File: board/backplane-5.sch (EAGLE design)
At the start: 146 parts, among them CN1 RJ45JACK90, CN2 4PINCONNFEMALE-1.6, CN3 4PINCONNFEMALE-1.6, CN4 4PINCONNFEMALE-1.6, CN5 4PINCONNFEMALE-1.6, CN6 4PINCONNFEMALE-1.6, U1 AMS1117-5.0, U10 RT9193, U11 KSZ9897, U12 KSZ8081MLX, U13 STM32F217-100, U2 AMS1117-5.0, U3 AMS1117-5.0, U4 AMS1117-5.0, U5 AMS1117-5.0, U6 AMS1117-2.5, U7 AMS1117-1.2, U8 RT9193, U9 AMS1117-5.0, Y1 25MHz, Y2 25MHz, Y3 25MHz

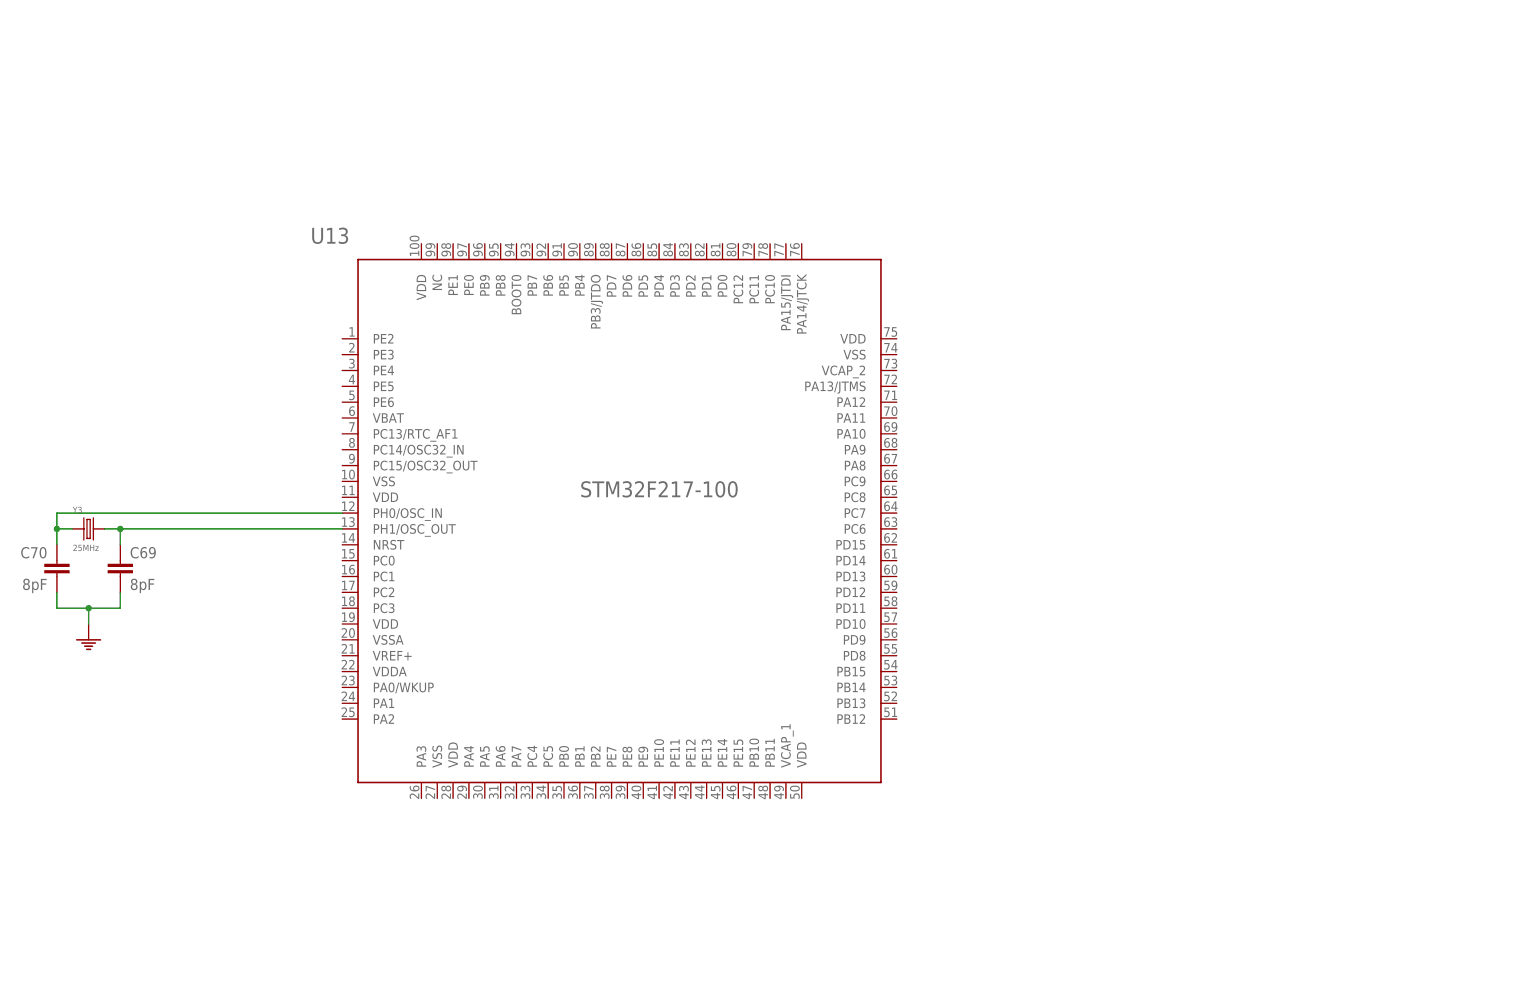
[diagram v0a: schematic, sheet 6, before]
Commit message: Added power to the STM32 and its decoupling caps
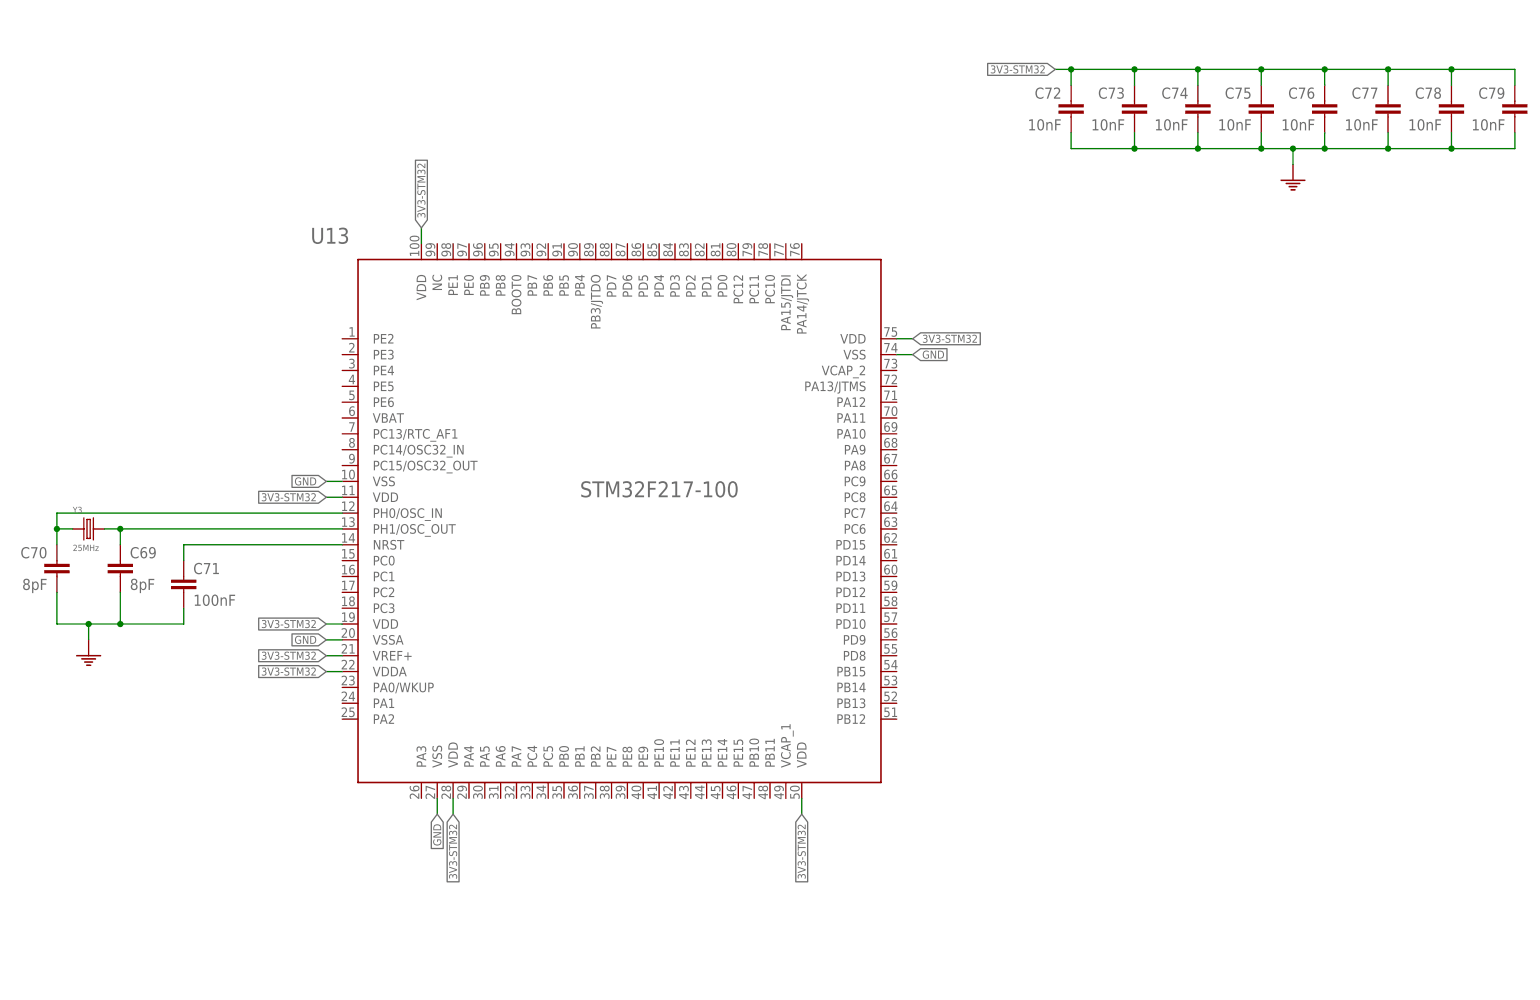
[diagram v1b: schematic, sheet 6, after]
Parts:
- added C71: 100nF, tuetuopay:C0603
- added C72, C73, C74, C75, C76, C77, C78, C79: 10nF, tuetuopay:C0603
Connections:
- new net N$23: C71.1, U13.NRST
- net 3V3-STM32: now also C72.1, C73.1, C74.1, C75.1, C76.1, C77.1, C78.1, C79.1, U13.VDD@1, U13.VDD@2, U13.VDD@3, U13.VDD@4, U13.VDD@5, U13.VDD@6, U13.VDDA@1, U13.VREF+
- net GND: now also C71.2, C72.2, C73.2, C74.2, C75.2, C76.2, C77.2, C78.2, C79.2, U13.VSS@1, U13.VSS@2, U13.VSS@3, U13.VSSA@1

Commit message: Added VCAP capacitors
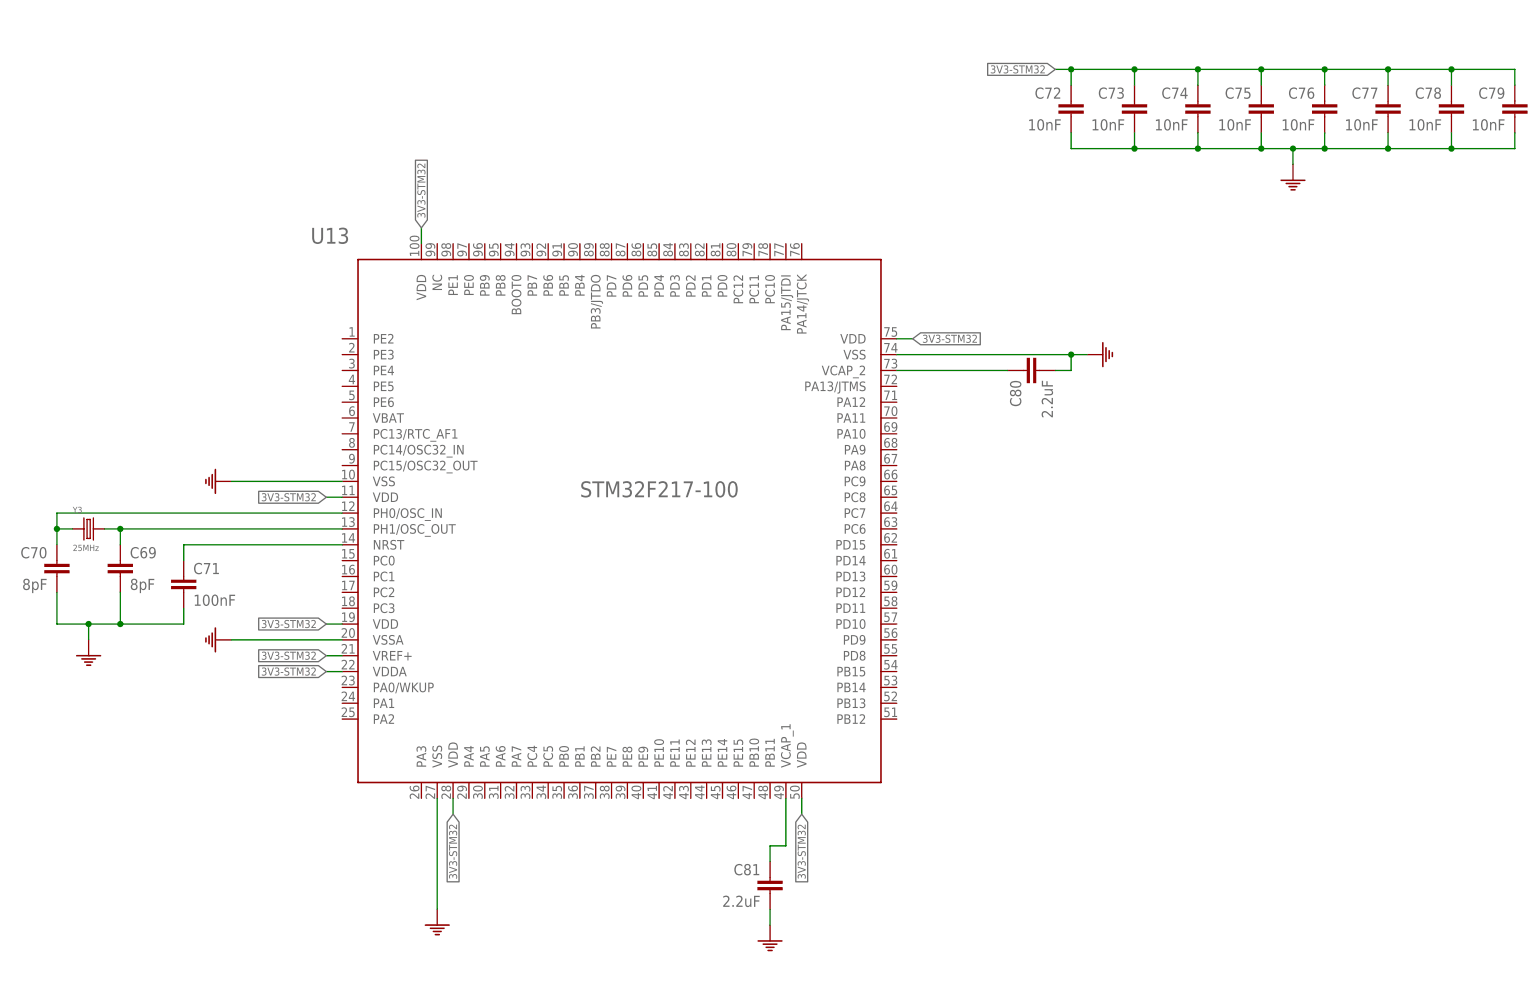
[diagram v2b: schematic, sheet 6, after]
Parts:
- added C80, C81: 2.2uF, tuetuopay:C0805
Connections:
- new net N$34: C80.1, U13.VCAP_2
- new net N$35: C81.1, U13.VCAP_1
- net GND: now also C80.2, C81.2

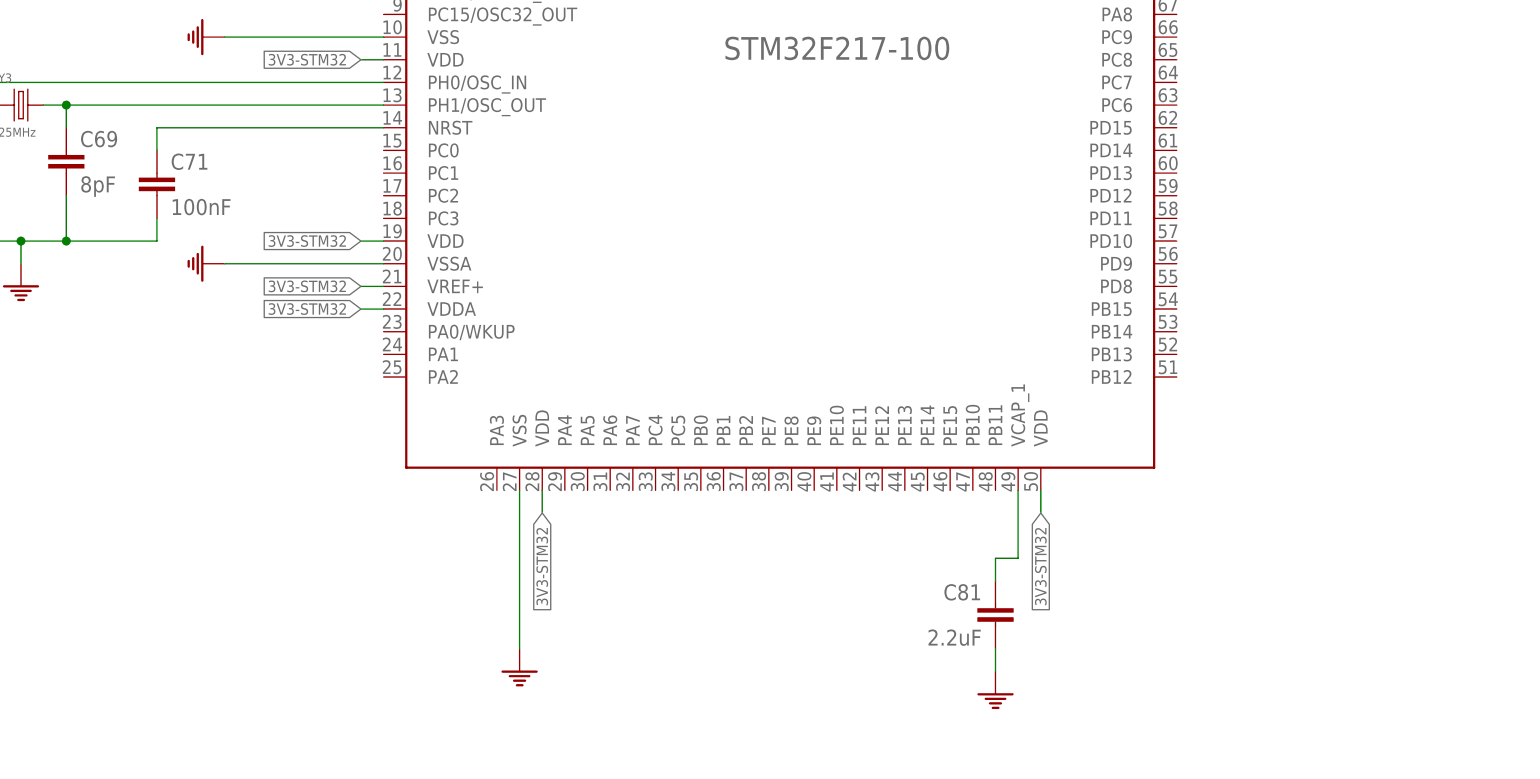
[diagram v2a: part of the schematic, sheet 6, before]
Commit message: Added switch <-> stm32 rmii in schematic
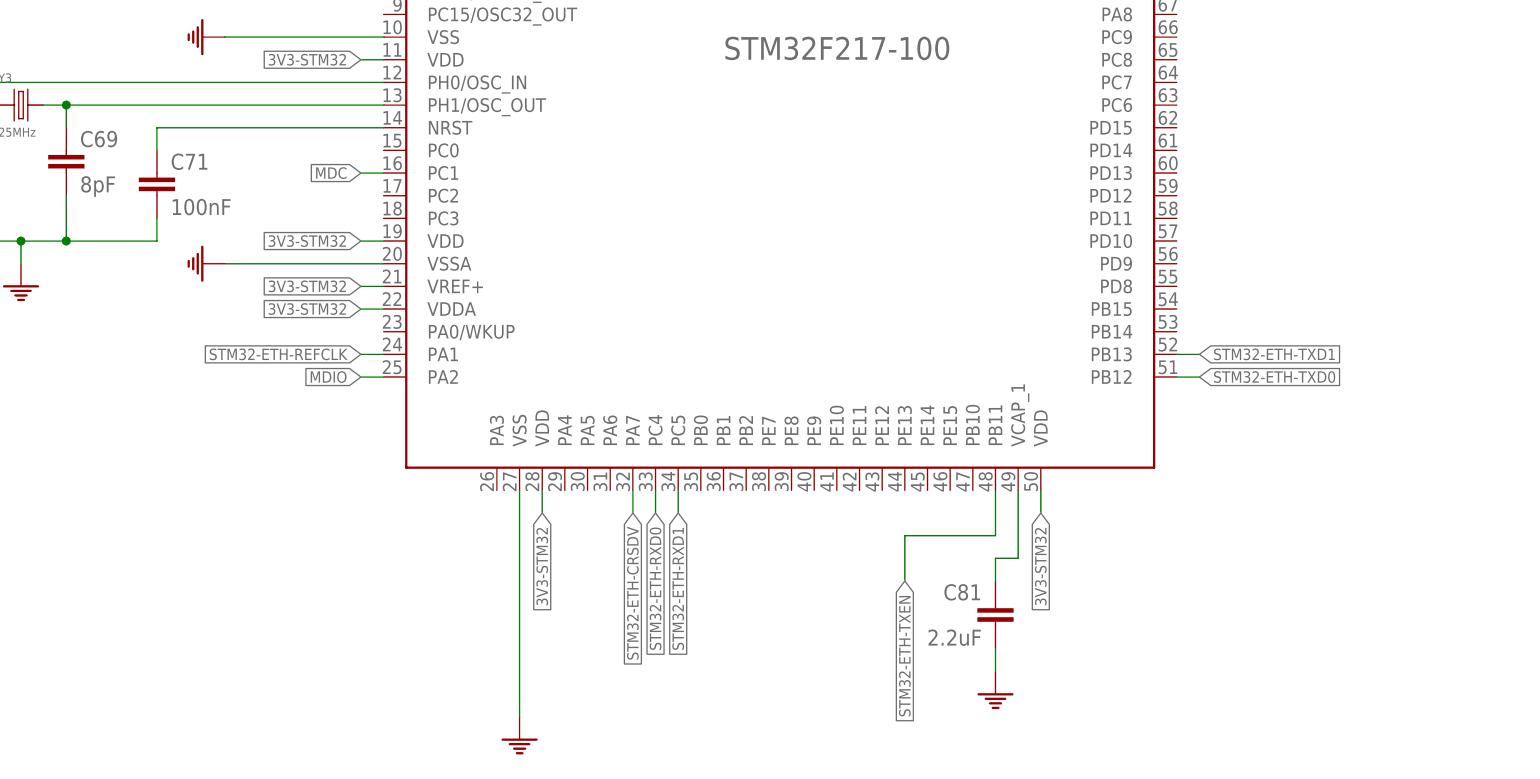
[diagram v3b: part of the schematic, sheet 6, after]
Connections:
- new net STM32-ETH-CRSDV: U11.RX_DV7/CRS_DV7/RX_CTL7, U13.PA7
- new net STM32-ETH-REFCLK: U11.TX_CLK7/REFCLKI7, U13.PA1
- new net STM32-ETH-RXD0: U11.RXD7_0, U13.PC4
- new net STM32-ETH-RXD1: U11.RXD7_1, U13.PC5
- new net STM32-ETH-TXD0: U11.TXD7_0, U13.PB12
- new net STM32-ETH-TXD1: U11.TXD7_1, U13.PB13
- new net STM32-ETH-TXEN: U11.TX_EN7/TX_CTL7, U13.PB11
- net MDC: now also U13.PC1
- net MDIO: now also U13.PA2

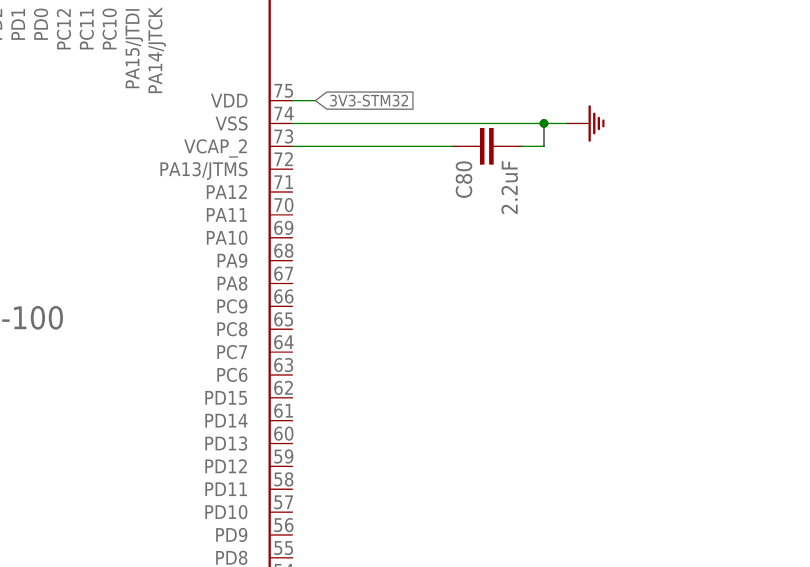
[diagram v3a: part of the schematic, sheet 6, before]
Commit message: Added the REFCLK source for switch <-> stm
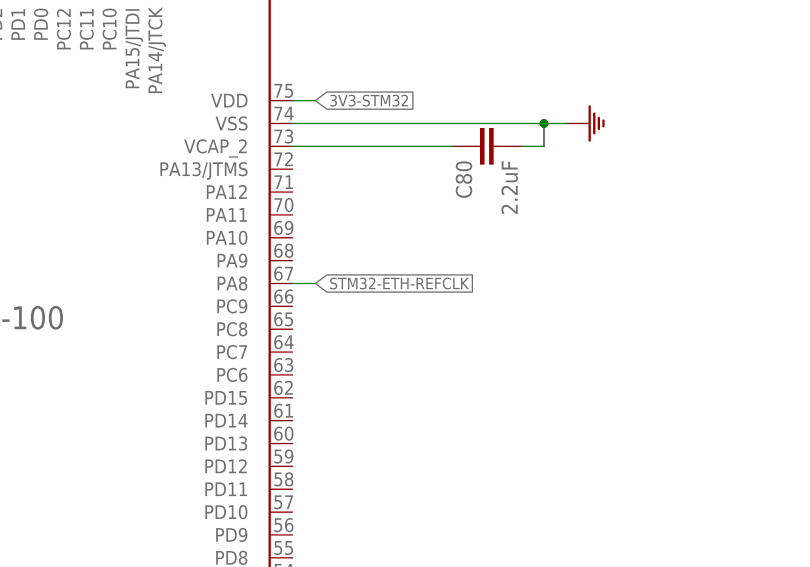
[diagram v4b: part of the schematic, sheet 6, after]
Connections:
- net STM32-ETH-REFCLK: now also U13.PA8
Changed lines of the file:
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@@
 <label x="60.96" y="66.04" size="1.27" layer="95" rot="R180" xref="yes"/>
+</segment>
+<segment>
+<pinref part="U13" gate="G$1" pin="PA8"/>
+<wire x1="152.4" y1="104.14" x2="154.94" y2="104.14" width="0.1524" layer="91"/>
+<label x="154.94" y="104.14" size="1.27" layer="95" xref="yes"/>
 </segment>
 </net>

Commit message: Proper supply symbols for some supply rails
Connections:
- net 12V renamed +12V
- net 5V renamed +5V
- removed net 2V5: C11.POS, C54.1, C55.1, C56.1, C57.1, C61.1, C62.1, L2.2, LED1.A, LED10.A, LED2.A, LED3.A, LED4.A, LED5.A, LED6.A, LED7.A, LED8.A, LED9.A, R16.2, R29.1, R30.1, R31.1, R32.2, R4.2, R7.2, R8.2, U11.VDDIO, U12.VDDIO, U6.VOUT
- new net VCCIO: C11.POS, C54.1, C55.1, C56.1, C57.1, C61.1, C62.1, C72.1, C73.1, C74.1, C75.1, C76.1, C77.1, C78.1, C79.1, L2.2, LED1.A, LED10.A, LED2.A, LED3.A, LED4.A, LED5.A, LED6.A, LED7.A, LED8.A, LED9.A, R16.2, R29.1, R30.1, R31.1, R32.2, R4.2, R6.2, R7.2, R8.2, U11.VDDIO, U12.VDDIO, U13.VDD@1, U13.VDD@2, U13.VDD@3, U13.VDD@4, U13.VDD@5, U13.VDD@6, U13.VDDA@1, U13.VREF+, U6.VOUT
- net 3V3-PHY: no longer R6.2
- net 3V3-STM32: no longer C72.1, C73.1, C74.1, C75.1, C76.1, C77.1, C78.1, C79.1, U13.VDD@1, U13.VDD@2, U13.VDD@3, U13.VDD@4, U13.VDD@5, U13.VDD@6, U13.VDDA@1, U13.VREF+
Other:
- moved on the sheet: C72, C73, C74, C75, C76, C77, C78, C79, C80, C81

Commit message: Wired Pis in Gbps and used PHY for ext jack
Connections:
- removed net PHY1->PI1_N: RJ1.3, U11.TXRX1M_B
- removed net PHY1->PI1_P: RJ1.6, U11.TXRX1P_B
- removed net PHY2->PI2_N: RJ2.3, U11.TXRX2M_B
- removed net PHY2->PI2_P: RJ2.6, U11.TXRX2P_B
- removed net PHY3->PI3_N: RJ3.3, U11.TXRX3M_B
- removed net PHY3->PI3_P: RJ3.6, U11.TXRX3P_B
- removed net PHY4->PI4_N: RJ4.3, U11.TXRX4M_B
- removed net PHY4->PI4_P: RJ4.6, U11.TXRX4P_B
- removed net PHY6->PI5_N: RJ5.3, U12.RXM
- removed net PHY6->PI5_P: RJ5.6, U12.RXP
- removed net PI1->PHY1_N: RJ1.7, U11.TXRX1M_A
- removed net PI1->PHY1_P: RJ1.8, U11.TXRX1P_A
- removed net PI2->PHY2_N: RJ2.7, U11.TXRX2M_A
- removed net PI2->PHY2_P: RJ2.8, U11.TXRX2P_A
- removed net PI3->PHY3_N: RJ3.7, U11.TXRX3M_A
- removed net PI3->PHY3_P: RJ3.8, U11.TXRX3P_A
- removed net PI4->PHY4_N: RJ4.7, U11.TXRX4M_A
- removed net PI4->PHY4_P: RJ4.8, U11.TXRX4P_A
- removed net PI5->PHY6_N: RJ5.7, U12.TXM
- removed net PI5->PHY6_P: RJ5.8, U12.TXP
- new net PHY1A_N: RJ1.2, U11.TXRX1M_A
- new net PHY1A_P: RJ1.1, U11.TXRX1P_A
- new net PHY1B_N: RJ1.6, U11.TXRX1M_B
- new net PHY1B_P: RJ1.3, U11.TXRX1P_B
- new net PHY1C_N: RJ1.5, U11.TXRX1M_C
- new net PHY1C_P: RJ1.4, U11.TXRX1P_C
- new net PHY1D_N: RJ1.8, U11.TXRX1M_D
- new net PHY1D_P: RJ1.7, U11.TXRX1P_D
- new net PHY2A_N: RJ2.2, U11.TXRX2M_A
- new net PHY2A_P: RJ2.1, U11.TXRX2P_A
- new net PHY2B_N: RJ2.6, U11.TXRX2M_B
- new net PHY2B_P: RJ2.3, U11.TXRX2P_B
- new net PHY2C_N: RJ2.5, U11.TXRX2M_C
- new net PHY2C_P: RJ2.4, U11.TXRX2P_C
- new net PHY2D_N: RJ2.8, U11.TXRX2M_D
- new net PHY2D_P: RJ2.7, U11.TXRX2P_D
- new net PHY3A_N: RJ3.2, U11.TXRX3M_A
- new net PHY3A_P: RJ3.1, U11.TXRX3P_A
- new net PHY3B_N: RJ3.6, U11.TXRX3M_B
- new net PHY3B_P: RJ3.3, U11.TXRX3P_B
- new net PHY3C_N: RJ3.5, U11.TXRX3M_C
- new net PHY3C_P: RJ3.4, U11.TXRX3P_C
- new net PHY3D_N: RJ3.8, U11.TXRX3M_D
- new net PHY3D_P: RJ3.7, U11.TXRX3P_D
- new net PHY4A_N: RJ4.2, U11.TXRX4M_A
- new net PHY4A_P: RJ4.1, U11.TXRX4P_A
- new net PHY4B_N: RJ4.6, U11.TXRX4M_B
- new net PHY4B_P: RJ4.3, U11.TXRX4P_B
- new net PHY4C_N: RJ4.5, U11.TXRX4M_C
- new net PHY4C_P: RJ4.4, U11.TXRX4P_C
- new net PHY4D_N: RJ4.8, U11.TXRX4M_D
- new net PHY4D_P: RJ4.7, U11.TXRX4P_D
- new net PHY6A_N: CN1.2, U12.RXM
- new net PHY6A_P: CN1.1, U12.RXP
- new net PHY6B_N: CN1.6, U12.TXM
- new net PHY6B_P: CN1.3, U12.TXP
- new net PHY6C_N: CN1.5
- new net PHY6C_P: CN1.4
- new net PHY6D_N: CN1.8
- new net PHY6D_P: CN1.7
- net PHY5A_N: now also RJ5.2; no longer CN1.2
- net PHY5A_P: now also RJ5.1; no longer CN1.1
- net PHY5B_N: now also RJ5.6; no longer CN1.6
- net PHY5B_P: now also RJ5.3; no longer CN1.3
- net PHY5C_N: now also RJ5.5; no longer CN1.5
- net PHY5C_P: now also RJ5.4; no longer CN1.4
- net PHY5D_N: now also RJ5.8; no longer CN1.8
- net PHY5D_P: now also RJ5.7; no longer CN1.7
- net PHY5LED0: now also R25.2; no longer CN1.YELLOW_C
- net PHY5LED1: now also R26.2; no longer CN1.GREEN_C
- net PHY6LED0: now also CN1.YELLOW_C; no longer R25.2
- net PHY6LED1: now also CN1.GREEN_C; no longer R26.2
